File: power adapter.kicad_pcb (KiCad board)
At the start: 2 copper layers, 63.5 x 38.1 mm, 8 parts

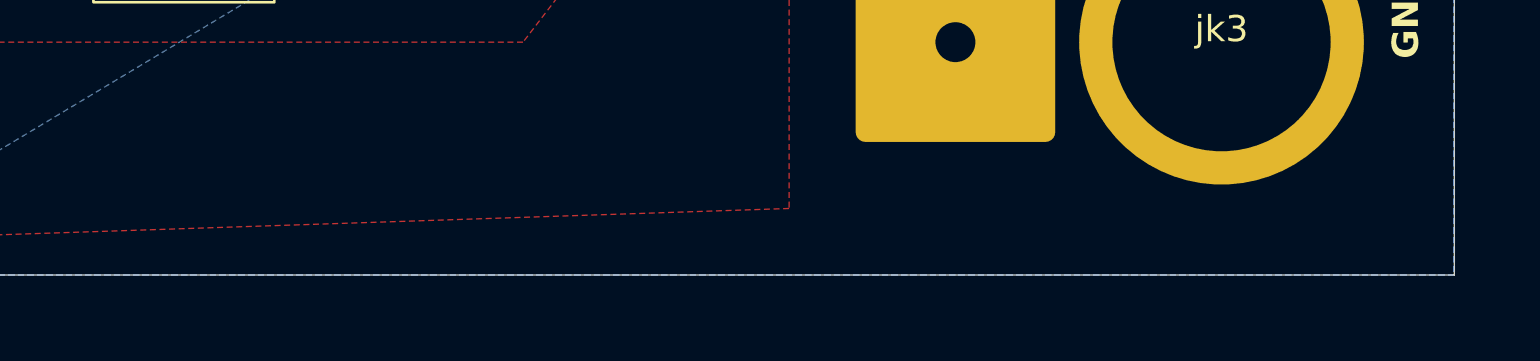
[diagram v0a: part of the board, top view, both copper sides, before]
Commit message: gold edge added
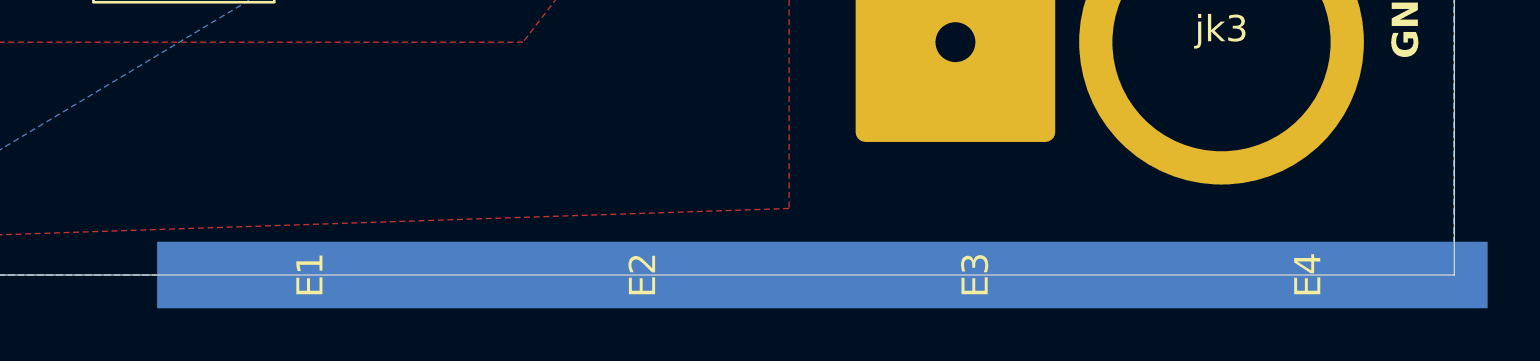
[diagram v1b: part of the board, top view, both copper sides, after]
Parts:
- added E1: ~, adpterpcblib:edge, F.Cu at (45.7, 114.3)
- added E2: ~, adpterpcblib:edge, F.Cu at (58.4, 114.3)
- added E3: ~, adpterpcblib:edge, F.Cu at (71.1, 114.3)
- added E4: ~, adpterpcblib:edge, F.Cu at (83.8, 114.3)

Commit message: added default widths
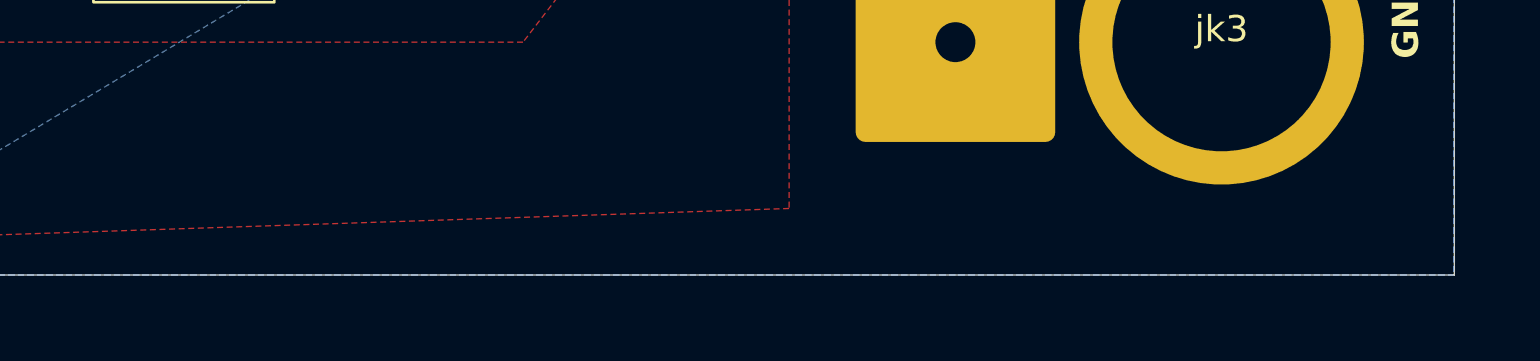
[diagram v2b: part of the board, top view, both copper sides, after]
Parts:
- removed E1, E2, E3, E4: ~, adpterpcblib:edge
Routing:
- removed copper zone on B.Cu, net +12V

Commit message: Mk2firstCommit
more attention paid to fixing ERCs
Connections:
- U1 pad 4: GND -> Net-(U1-Pin_4)
- U1 pad 6: GND -> Net-(U1-Pin_4)
- U1 pad 8: GND -> Net-(U1-Pin_4)
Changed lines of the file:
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@@
 	(net 2 "-12V")
 	(net 3 "+12V")
+	(net 4 "Net-(U1-Pin_4)")
 	(footprint "adapterpcblib:Banana"
 		(layer "F.Cu")
@@
 			)
 			(remove_unused_layers no)
-			(net 1 "GND")
+			(net 4 "Net-(U1-Pin_4)")
 			(pinfunction "Pin_4")
 			(pintype "power_in")
@@
 			)
 			(remove_unused_layers no)
-			(net 1 "GND")
+			(net 4 "Net-(U1-Pin_4)")
 			(pinfunction "Pin_6")
 			(pintype "power_in")
@@
 			)
 			(remove_unused_layers no)
-			(net 1 "GND")
+			(net 4 "Net-(U1-Pin_4)")
 			(pinfunction "Pin_8")
 			(pintype "power_in")
